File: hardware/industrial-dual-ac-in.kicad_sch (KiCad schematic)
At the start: 26 parts, among them P1 CON-SENSOR2, P2 BOOT, P3 Debug, P4 Input, U1 XMC1100, U109 HCPL2731

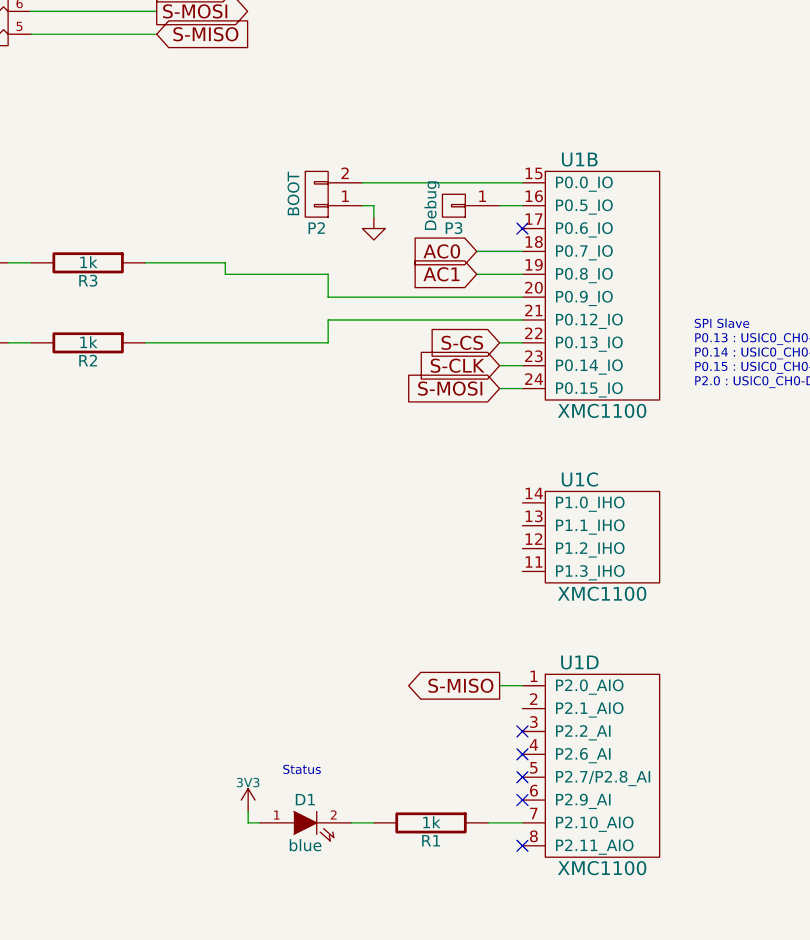
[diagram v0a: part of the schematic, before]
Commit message: more clearance for screwholes
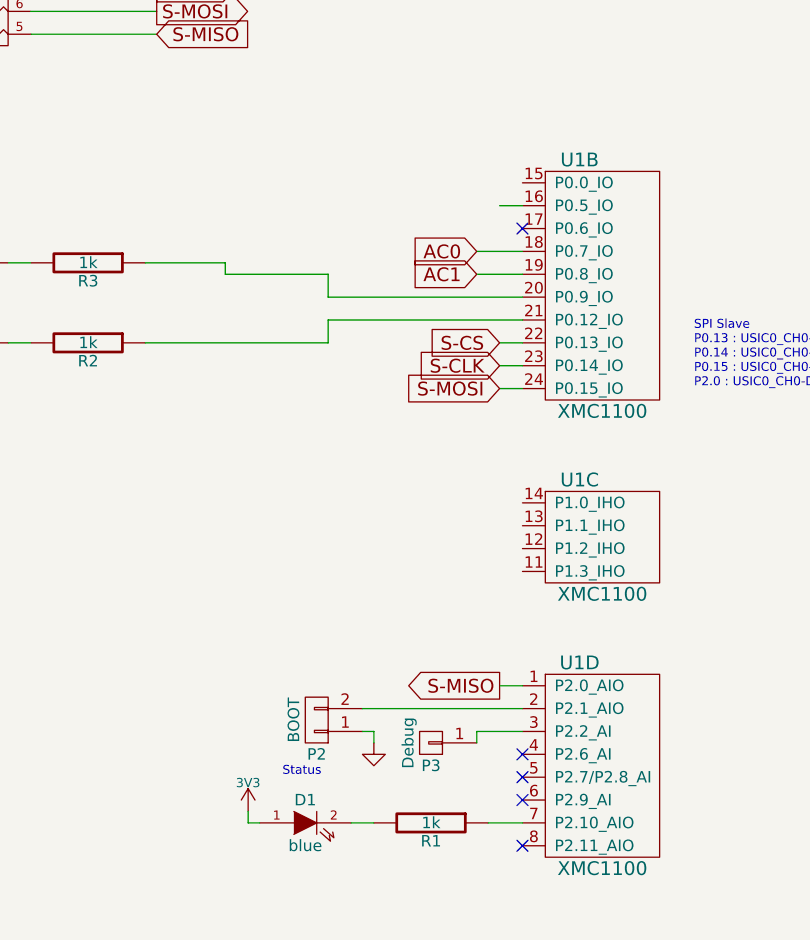
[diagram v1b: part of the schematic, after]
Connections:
- net at P3.1 (P1): now also U1.3 (P2.2_AI); no longer U1.16 (P0.5_IO)
- net at U1.15 (P0.0_IO): no longer P2.2 (P2)
- net at U1.2 (P2.1_AIO): now also P2.2 (P2)
- no-connect marks 6 -> 5
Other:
- moved on the sheet: P2, P3
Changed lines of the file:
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@@
   (no_connect (at 116.84 129.54))
   (no_connect (at 116.84 127))
-  (no_connect (at 116.84 124.46))
   (no_connect (at 116.84 68.58))
   (wire (pts (xy 44.45 22.86) (xy 58.42 22.86))
     (stroke (width 0) (type default) (color 0 0 0 0))
   )
+  (wire (pts (xy 111.76 125.73) (xy 111.76 124.46))
+    (stroke (width 0) (type default) (color 0 0 0 0))
+  )
   (wire (pts (xy 95.25 78.74) (xy 116.84 78.74))
     (stroke (width 0) (type default) (color 0 0 0 0))
@@
     (stroke (width 0) (type default) (color 0 0 0 0))
   )
-  (wire (pts (xy 99.06 63.5) (xy 116.84 63.5))
+  (wire (pts (xy 99.06 121.92) (xy 116.84 121.92))
     (stroke (width 0) (type default) (color 0 0 0 0))
   )
@@
     (stroke (width 0) (type default) (color 0 0 0 0))
   )
-  (wire (pts (xy 100.33 66.04) (xy 100.33 67.31))
+  (wire (pts (xy 100.33 124.46) (xy 100.33 125.73))
     (stroke (width 0) (type default) (color 0 0 0 0))
   )
@@
     (stroke (width 0) (type default) (color 0 0 0 0))
   )
-  (wire (pts (xy 99.06 66.04) (xy 100.33 66.04))
+  (wire (pts (xy 99.06 124.46) (xy 100.33 124.46))
     (stroke (width 0) (type default) (color 0 0 0 0))
   )
@@
   )
   (wire (pts (xy 76.2 41.91) (xy 62.23 41.91))
+    (stroke (width 0) (type default) (color 0 0 0 0))
+  )
+  (wire (pts (xy 111.76 124.46) (xy 116.84 124.46))
     (stroke (width 0) (type default) (color 0 0 0 0))
   )
@@
     (pin "2")
   )
-  (symbol (lib_id "tinkerforge:CONN_01X01") (at 109.22 66.04 180) (unit 1)
-    (in_bom yes) (on_board yes)
-    (property "Reference" "P3" (id 0) (at 109.22 68.58 0))
-    (property "Value" "Debug" (id 1) (at 106.68 66.04 90))
-    (property "Footprint" "kicad-libraries:DEBUG_PAD" (id 2) (at 109.22 66.04 0)
-      (effects (font (size 1.27 1.27)) hide)
-    )
-    (property "Datasheet" "" (id 3) (at 109.22 66.04 0))
+  (symbol (lib_id "tinkerforge:CONN_01X01") (at 106.68 125.73 180) (unit 1)
+    (in_bom yes) (on_board yes)
+    (property "Reference" "P3" (id 0) (at 106.68 128.27 0))
+    (property "Value" "Debug" (id 1) (at 104.14 125.73 90))
+    (property "Footprint" "kicad-libraries:DEBUG_PAD" (id 2) (at 106.68 125.73 0)
+      (effects (font (size 1.27 1.27)) hide)
+    )
+    (property "Datasheet" "" (id 3) (at 106.68 125.73 0))
     (pin "1")
   )
@@
     (pin "2")
   )
-  (symbol (lib_id "tinkerforge:CONN_01X02") (at 93.98 64.77 180) (unit 1)
-    (in_bom yes) (on_board yes)
-    (property "Reference" "P2" (id 0) (at 93.98 68.58 0))
-    (property "Value" "BOOT" (id 1) (at 91.44 64.77 90))
-    (property "Footprint" "kicad-libraries:SolderJumper" (id 2) (at 93.98 62.23 0)
-      (effects (font (size 1.27 1.27)) hide)
-    )
-    (property "Datasheet" "" (id 3) (at 93.98 62.23 0))
+  (symbol (lib_id "tinkerforge:CONN_01X02") (at 93.98 123.19 180) (unit 1)
+    (in_bom yes) (on_board yes)
+    (property "Reference" "P2" (id 0) (at 93.98 127 0))
+    (property "Value" "BOOT" (id 1) (at 91.44 123.19 90))
+    (property "Footprint" "kicad-libraries:SolderJumper" (id 2) (at 93.98 120.65 0)
+      (effects (font (size 1.27 1.27)) hide)
+    )
+    (property "Datasheet" "" (id 3) (at 93.98 120.65 0))
     (pin "1")
     (pin "2")
@@
     (pin "2")
   )
-  (symbol (lib_id "tinkerforge:GND") (at 100.33 67.31 0) (unit 1)
-    (in_bom yes) (on_board yes)
-    (property "Reference" "#PWR07" (id 0) (at 100.33 67.31 0)
+  (symbol (lib_id "tinkerforge:GND") (at 100.33 125.73 0) (unit 1)
+    (in_bom yes) (on_board yes)
+    (property "Reference" "#PWR07" (id 0) (at 100.33 125.73 0)
       (effects (font (size 0.762 0.762)) hide)
     )
-    (property "Value" "GND" (id 1) (at 100.33 69.088 0)
+    (property "Value" "GND" (id 1) (at 100.33 127.508 0)
       (effects (font (size 0.762 0.762)) hide)
     )
-    (property "Footprint" "" (id 2) (at 100.33 67.31 0)
-      (effects (font (size 1.524 1.524)) hide)
-    )
-    (property "Datasheet" "" (id 3) (at 100.33 67.31 0)
-      (effects (font (size 1.524 1.524)) hide)
-    )
+    (property "Footprint" "" (id 2) (at 100.33 125.73 0)
+      (effects (font (size 1.524 1.524)) hide)
+    )
+    (property "Datasheet" "" (id 3) (at 100.33 125.73 0)
+      (effects (font (size 1.524 1.524)) hide)
+    )

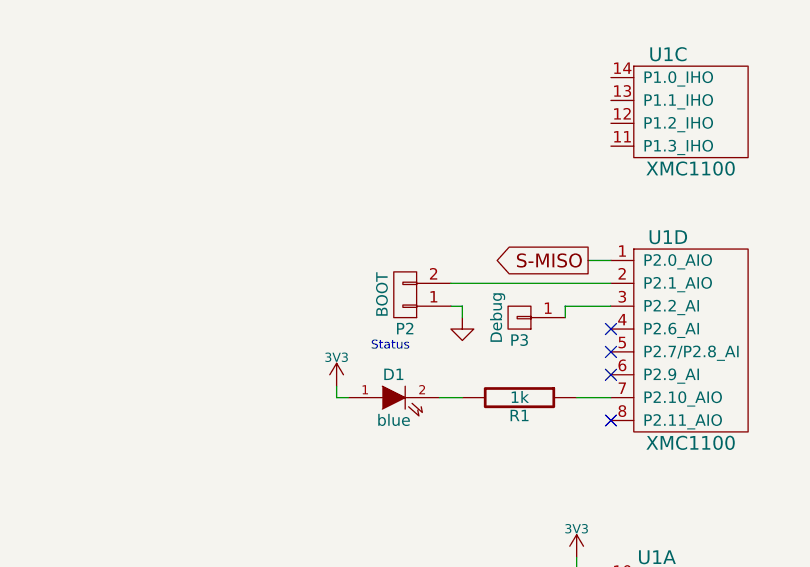
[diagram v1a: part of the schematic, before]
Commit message: switched debug an boot pin
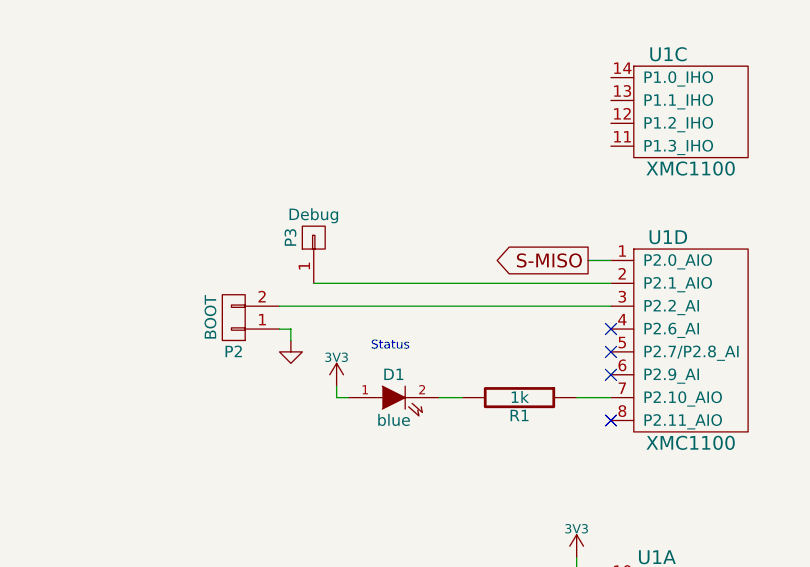
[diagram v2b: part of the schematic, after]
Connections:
- net at P3.1 (P1): now also U1.2 (P2.1_AIO); no longer U1.3 (P2.2_AI)
- net at P2.2 (P2): now also U1.3 (P2.2_AI); no longer U1.2 (P2.1_AIO)
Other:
- moved on the sheet: P2, P3
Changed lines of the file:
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@@
-    (stroke (width 0) (type default) (color 0 0 0 0))
-  )
-  (wire (pts (xy 111.76 125.73) (xy 111.76 124.46))
     (stroke (width 0) (type default) (color 0 0 0 0))
   )
@@
     (stroke (width 0) (type default) (color 0 0 0 0))
   )
-  (wire (pts (xy 99.06 121.92) (xy 116.84 121.92))
-    (stroke (width 0) (type default) (color 0 0 0 0))
-  )
   (wire (pts (xy 111.76 71.12) (xy 116.84 71.12))
     (stroke (width 0) (type default) (color 0 0 0 0))
@@
     (stroke (width 0) (type default) (color 0 0 0 0))
   )
-  (wire (pts (xy 100.33 124.46) (xy 100.33 125.73))
+  (wire (pts (xy 81.28 127) (xy 81.28 128.27))
     (stroke (width 0) (type default) (color 0 0 0 0))
   )
@@
     (stroke (width 0) (type default) (color 0 0 0 0))
   )
+  (wire (pts (xy 80.01 124.46) (xy 116.84 124.46))
+    (stroke (width 0) (type default) (color 0 0 0 0))
+  )
   (wire (pts (xy 294.64 69.85) (xy 302.26 69.85))
     (stroke (width 0) (type default) (color 0 0 0 0))
@@
     (stroke (width 0) (type default) (color 0 0 0 0))
   )
-  (wire (pts (xy 99.06 124.46) (xy 100.33 124.46))
+  (wire (pts (xy 80.01 127) (xy 81.28 127))
     (stroke (width 0) (type default) (color 0 0 0 0))
   )
@@
     (stroke (width 0) (type default) (color 0 0 0 0))
   )
-  (wire (pts (xy 111.76 124.46) (xy 116.84 124.46))
-    (stroke (width 0) (type default) (color 0 0 0 0))
-  )
   (wire (pts (xy 233.68 80.01) (xy 227.33 80.01))
     (stroke (width 0) (type default) (color 0 0 0 0))
@@
   )
   (wire (pts (xy 41.91 44.45) (xy 52.07 44.45))
+    (stroke (width 0) (type default) (color 0 0 0 0))
+  )
+  (wire (pts (xy 83.82 121.92) (xy 116.84 121.92))
     (stroke (width 0) (type default) (color 0 0 0 0))
   )
@@
     (pin "2")
   )
-  (symbol (lib_id "tinkerforge:CONN_01X01") (at 106.68 125.73 180) (unit 1)
-    (in_bom yes) (on_board yes)
-    (property "Reference" "P3" (id 0) (at 106.68 128.27 0))
-    (property "Value" "Debug" (id 1) (at 104.14 125.73 90))
-    (property "Footprint" "kicad-libraries:DEBUG_PAD" (id 2) (at 106.68 125.73 0)
-      (effects (font (size 1.27 1.27)) hide)
-    )
-    (property "Datasheet" "" (id 3) (at 106.68 125.73 0))
+  (symbol (lib_id "tinkerforge:CONN_01X01") (at 83.82 116.84 90) (unit 1)
+    (in_bom yes) (on_board yes)
+    (property "Reference" "P3" (id 0) (at 81.28 116.84 0))
+    (property "Value" "Debug" (id 1) (at 83.82 114.3 90))
+    (property "Footprint" "kicad-libraries:DEBUG_PAD" (id 2) (at 83.82 116.84 0)
+      (effects (font (size 1.27 1.27)) hide)
+    )
+    (property "Datasheet" "" (id 3) (at 83.82 116.84 0))
     (pin "1")
   )
@@
     (pin "2")
   )
-  (symbol (lib_id "tinkerforge:CONN_01X02") (at 93.98 123.19 180) (unit 1)
-    (in_bom yes) (on_board yes)
-    (property "Reference" "P2" (id 0) (at 93.98 127 0))
-    (property "Value" "BOOT" (id 1) (at 91.44 123.19 90))
-    (property "Footprint" "kicad-libraries:SolderJumper" (id 2) (at 93.98 120.65 0)
-      (effects (font (size 1.27 1.27)) hide)
-    )
-    (property "Datasheet" "" (id 3) (at 93.98 120.65 0))
+  (symbol (lib_id "tinkerforge:CONN_01X02") (at 74.93 125.73 180) (unit 1)
+    (in_bom yes) (on_board yes)
+    (property "Reference" "P2" (id 0) (at 74.93 129.54 0))
+    (property "Value" "BOOT" (id 1) (at 72.39 125.73 90))
+    (property "Footprint" "kicad-libraries:SolderJumper" (id 2) (at 74.93 123.19 0)
+      (effects (font (size 1.27 1.27)) hide)
+    )
+    (property "Datasheet" "" (id 3) (at 74.93 123.19 0))
     (pin "1")
     (pin "2")
@@
     (pin "2")
   )
-  (symbol (lib_id "tinkerforge:GND") (at 100.33 125.73 0) (unit 1)
-    (in_bom yes) (on_board yes)
-    (property "Reference" "#PWR07" (id 0) (at 100.33 125.73 0)
+  (symbol (lib_id "tinkerforge:GND") (at 81.28 128.27 0) (unit 1)
+    (in_bom yes) (on_board yes)
+    (property "Reference" "#PWR07" (id 0) (at 81.28 128.27 0)
       (effects (font (size 0.762 0.762)) hide)
     )
-    (property "Value" "GND" (id 1) (at 100.33 127.508 0)
+    (property "Value" "GND" (id 1) (at 81.28 130.048 0)
       (effects (font (size 0.762 0.762)) hide)
     )
-    (property "Footprint" "" (id 2) (at 100.33 125.73 0)
-      (effects (font (size 1.524 1.524)) hide)
-    )
-    (property "Datasheet" "" (id 3) (at 100.33 125.73 0)
-      (effects (font (size 1.524 1.524)) hide)
-    )
+    (property "Footprint" "" (id 2) (at 81.28 128.27 0)
+      (effects (font (size 1.524 1.524)) hide)
+    )
+    (property "Datasheet" "" (id 3) (at 81.28 128.27 0)
+      (effects (font (size 1.524 1.524)) hide)
+    )

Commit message: updated mounting holes
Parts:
- Drill1, Drill2, Drill3, Drill4: footprint kicad-libraries:DRILL_NP_35 -> kicad-libraries:DRILL_NP
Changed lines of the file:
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@@
       (effects (font (size 1.524 1.524)) (justify left))
     )
-    (property "Footprint" "kicad-libraries:DRILL_NP_35" (id 2) (at 397.51 242.57 0)
+    (property "Footprint" "kicad-libraries:DRILL_NP" (id 2) (at 397.51 242.57 0)
       (effects (font (size 1.524 1.524)) hide)
     )
@@
       (effects (font (size 1.524 1.524)) (justify left))
     )
-    (property "Footprint" "kicad-libraries:DRILL_NP_35" (id 2) (at 389.89 242.57 0)
+    (property "Footprint" "kicad-libraries:DRILL_NP" (id 2) (at 389.89 242.57 0)
       (effects (font (size 1.524 1.524)) hide)
     )
@@
       (effects (font (size 1.524 1.524)) (justify left))
     )
-    (property "Footprint" "kicad-libraries:DRILL_NP_35" (id 2) (at 397.51 247.65 0)
+    (property "Footprint" "kicad-libraries:DRILL_NP" (id 2) (at 397.51 247.65 0)
       (effects (font (size 1.524 1.524)) hide)
     )
@@
       (effects (font (size 1.524 1.524)) (justify left))
     )
-    (property "Footprint" "kicad-libraries:DRILL_NP_35" (id 2) (at 389.89 247.65 0)
+    (property "Footprint" "kicad-libraries:DRILL_NP" (id 2) (at 389.89 247.65 0)
       (effects (font (size 1.524 1.524)) hide)
     )
@@
     )
     (path "/39b867dc-b423-4b46-b955-173069e1018d"
-      (reference "Drill1") (unit 1) (value "DRILL") (footprint "kicad-libraries:DRILL_NP_35")
+      (reference "Drill1") (unit 1) (value "DRILL") (footprint "kicad-libraries:DRILL_NP")
     )
     (path "/8464b325-aeb6-4638-8813-cab3f0549ee3"
-      (reference "Drill2") (unit 1) (value "DRILL") (footprint "kicad-libraries:DRILL_NP_35")
+      (reference "Drill2") (unit 1) (value "DRILL") (footprint "kicad-libraries:DRILL_NP")
     )
     (path "/26400ce2-b5fb-4141-92fe-1874c8c121a9"
-      (reference "Drill3") (unit 1) (value "DRILL") (footprint "kicad-libraries:DRILL_NP_35")
+      (reference "Drill3") (unit 1) (value "DRILL") (footprint "kicad-libraries:DRILL_NP")
     )
     (path "/5fc0d057-b2c9-4e2f-913e-66de6c4cc2f5"
-      (reference "Drill4") (unit 1) (value "DRILL") (footprint "kicad-libraries:DRILL_NP_35")
+      (reference "Drill4") (unit 1) (value "DRILL") (footprint "kicad-libraries:DRILL_NP")
     )
     (path "/3b0627a1-99af-4b4e-a60a-f20a843a44a0"
